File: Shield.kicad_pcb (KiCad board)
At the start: 4 copper layers, 162 x 99.6 mm, 93 parts, among them J1 SAMTEC-FTS-130-01-X-DV, J11 USB_C_Receptacle_PowerOnly_6P, J12 SIM_Card_Shielded, J13 Conn_02x03_Odd_Even, J14 USB3_A, J15 USB3_A, J2 SAMTEC-FTS-130-01-X-DV, J3 5051102291, J4 5051102291, J5 77313-118-40LF, J6 Bus_PCI_Express_Mini, J7 USB_C_Receptacle, J8 Bus_PCI_Express_Mini, J9 USB3_A, Q1 2N3904, Q2 MMBT3904, Q3 MMBT3904, U1 TCA9406DCUR, U10 AP62300Z6-7, U2 USB5744_2G, U3 AMS1117-3.3, U4 AMS1117-3.3, U5 AMS1117-1.8, U6 LM1117S-1.2, U7 TPS2051BDBVR, U8 TPS2051BDBVR, U9 TPS2051BDBVR, Y1 Crystal

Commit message: Added UART for LTE<->MCU
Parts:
- added U11: TXB0102DCUR, TXB0102DCUR:DCU0008A_N, F.Cu at (69.2, 83.0)
- J11: footprint U262-061N-4BVC10:U262-061N-4BVC10_XKB -> Type C 6 pin_ul_U262-061N-4BVC10:U262-061N-4BVC10_XKB
- moved D2 4.30 mm to (75.7, 81.2), turned to 0 degrees
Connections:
- J2 pad 22: /MCU_OPAMP1_VINP / PA0 -> /MCU_PA0 UART4_TX AF8
- J2 pad 24: /MCU_OPAMP1_VINM / PA1 -> /MCU_PA1 UART4_RX AF8
- J2 pad 51: /SOC_GPIO_28_PWM -> unconnected-(J2-Pad51)
- J5 pad 22: /MCU_OPAMP1_VINP / PA0 -> unconnected-(J5-Pad22)
- J5 pad 24: /MCU_OPAMP1_VINM / PA1 -> unconnected-(J5-Pad24)
- J8 pad 17: unconnected-(J8-UIM_C8-Pad17) -> /LTE_UART_TXD
- J8 pad 19: unconnected-(J8-UIM_C4-Pad19) -> /LTE_UART_RXD
- LED1 pad 3-GND: unconnected-(LED1-GND-Pad3-GND) -> GND
- U5 pad 1: unconnected-(U5-GND-Pad1) -> GND
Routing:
- net /LTE_UART_RXD: track 0.00 -> 106.3 mm, vias 0 -> 4
- net /LTE_UART_TXD: track 0.00 -> 101.0 mm, vias 0 -> 4
- net /1V8: track 29.9 -> 82.0 mm, vias 0 -> 2
- net /MCU_PA0 UART4_TX AF8: track 0.00 -> 37.8 mm
- net /MCU_PA1 UART4_RX AF8: track 0.00 -> 34.1 mm, vias 0 -> 2
- net /MCU_OPAMP1_VINM / PA1: track 29.1 -> 0.00 mm, vias 1 -> 0
- net /MCU_OPAMP1_VINP / PA0: track 28.6 -> 0.00 mm, vias 1 -> 0
- net VDD33: track 106.1 -> 121.9 mm, vias 5 -> 7
- net VDD12: track 62.4 -> 63.5 mm
- net GND: track 53.8 -> 53.1 mm, vias 27 -> 34

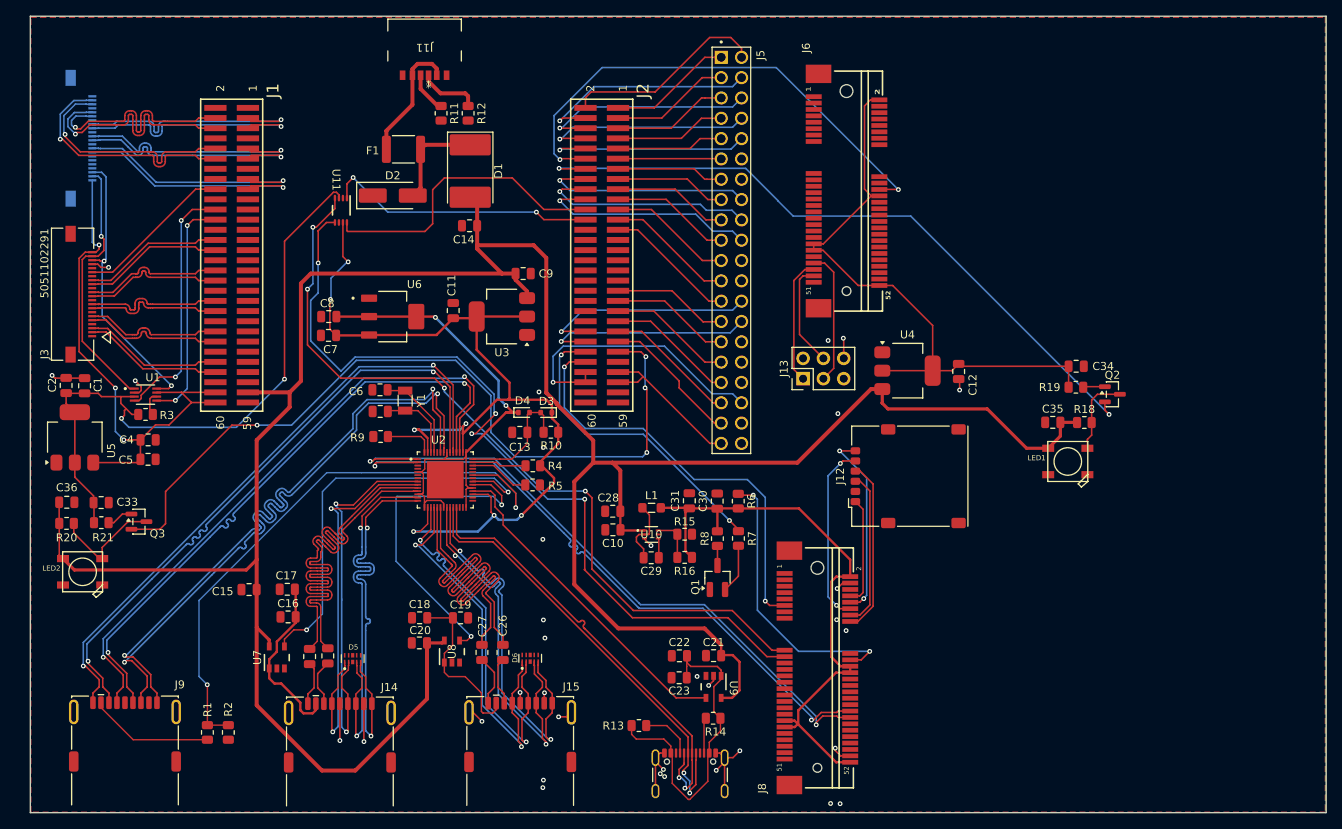
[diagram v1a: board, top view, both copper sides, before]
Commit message: Updated differential routing etc.
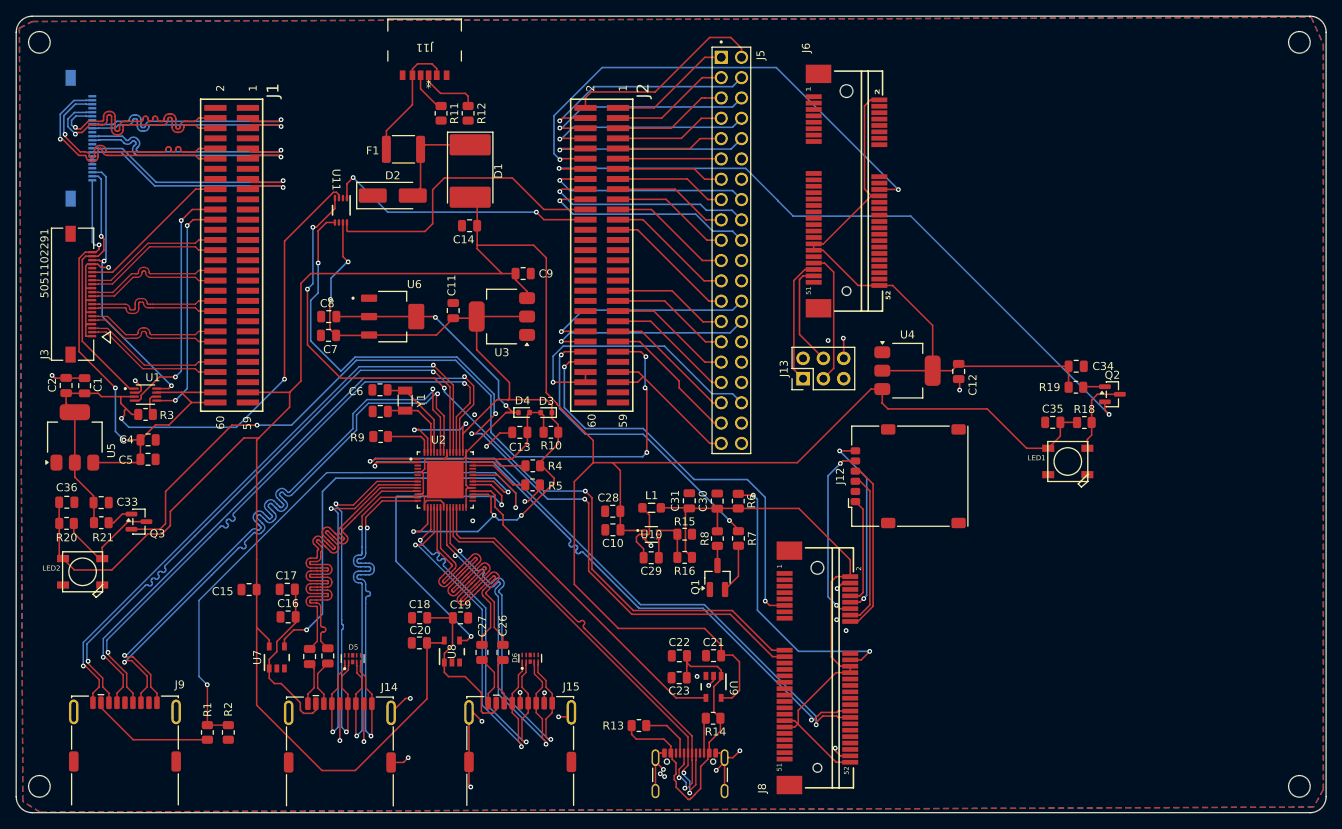
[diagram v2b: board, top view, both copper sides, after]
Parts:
- added REF**: MountingHole_2.7mm_M2.5_ISO14580, MountingHole:MountingHole_2.7mm_M2.5_ISO14580, F.Cu at (189.0, 62.0)
- added REF**: MountingHole_2.7mm_M2.5_ISO14580, MountingHole:MountingHole_2.7mm_M2.5_ISO14580, F.Cu at (189.0, 155.0)
- added REF**: MountingHole_2.7mm_M2.5_ISO14580, MountingHole:MountingHole_2.7mm_M2.5_ISO14580, F.Cu at (31.5, 62.0)
- added REF**: MountingHole_2.7mm_M2.5_ISO14580, MountingHole:MountingHole_2.7mm_M2.5_ISO14580, F.Cu at (31.5, 155.0)
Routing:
- net GND: track 53.1 -> 88.6 mm, vias 34 -> 31
- net /5V-VBUS: track 343.3 -> 350.9 mm
- net /DSI_D0+: track 28.6 -> 30.2 mm
- net /DSI_D1+: track 28.6 -> 30.1 mm
- net /DN2_TX-: track 54.0 -> 54.8 mm
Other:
- board size 162 x 99.6 mm -> 163.7 x 99.6 mm
